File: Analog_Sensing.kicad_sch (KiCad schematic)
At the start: 3 parts, among them U12 TMP1075NDRLR

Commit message: Layout draft complete
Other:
- note removed: "Analog Inputs - NOT NEEDED"
- title: (none) -> Jakka1
- moved on the sheet: C60, R48, U12

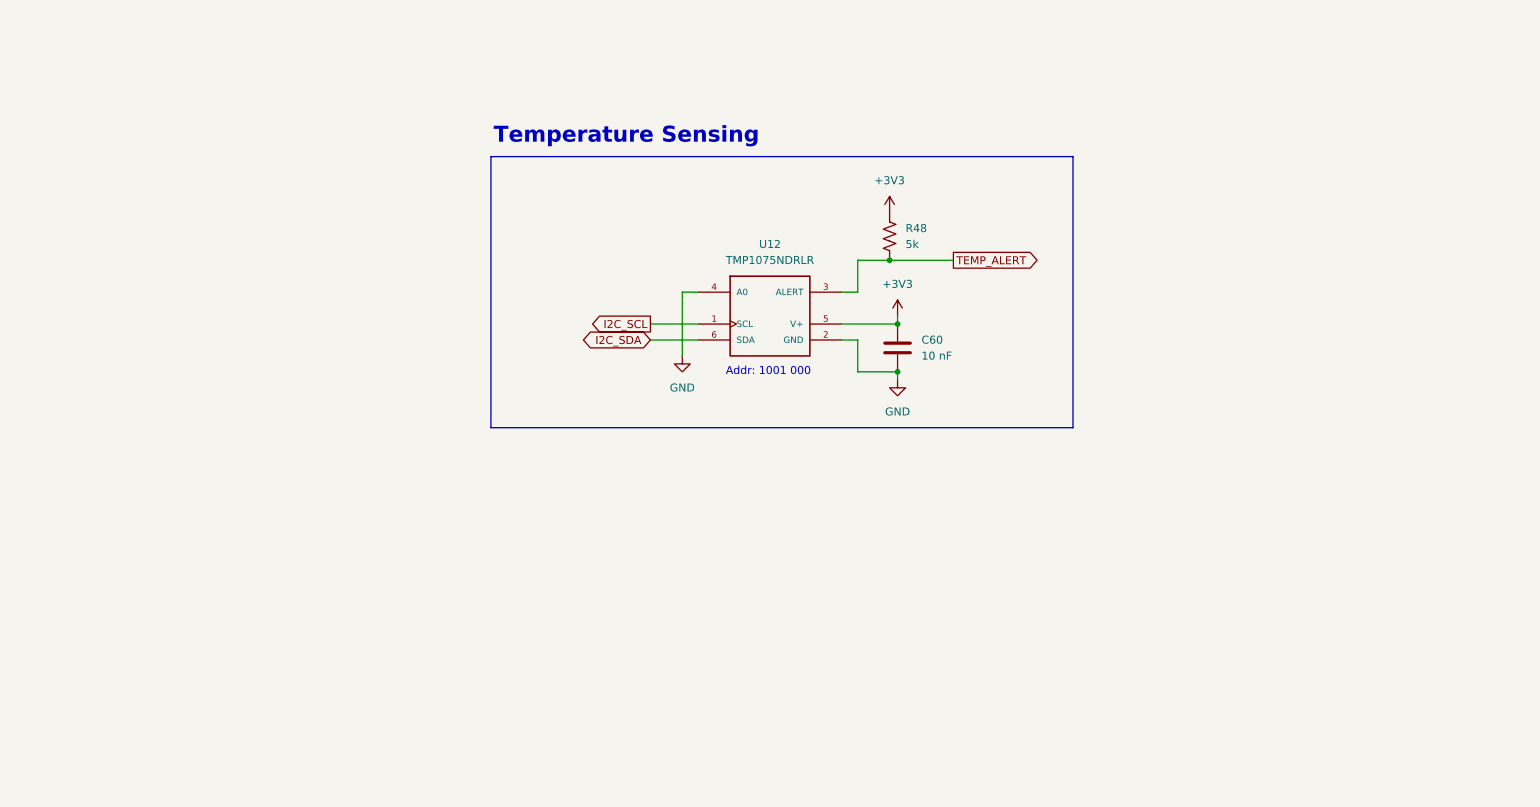
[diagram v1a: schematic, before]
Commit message: First draft of design output, schematic, and layout complete
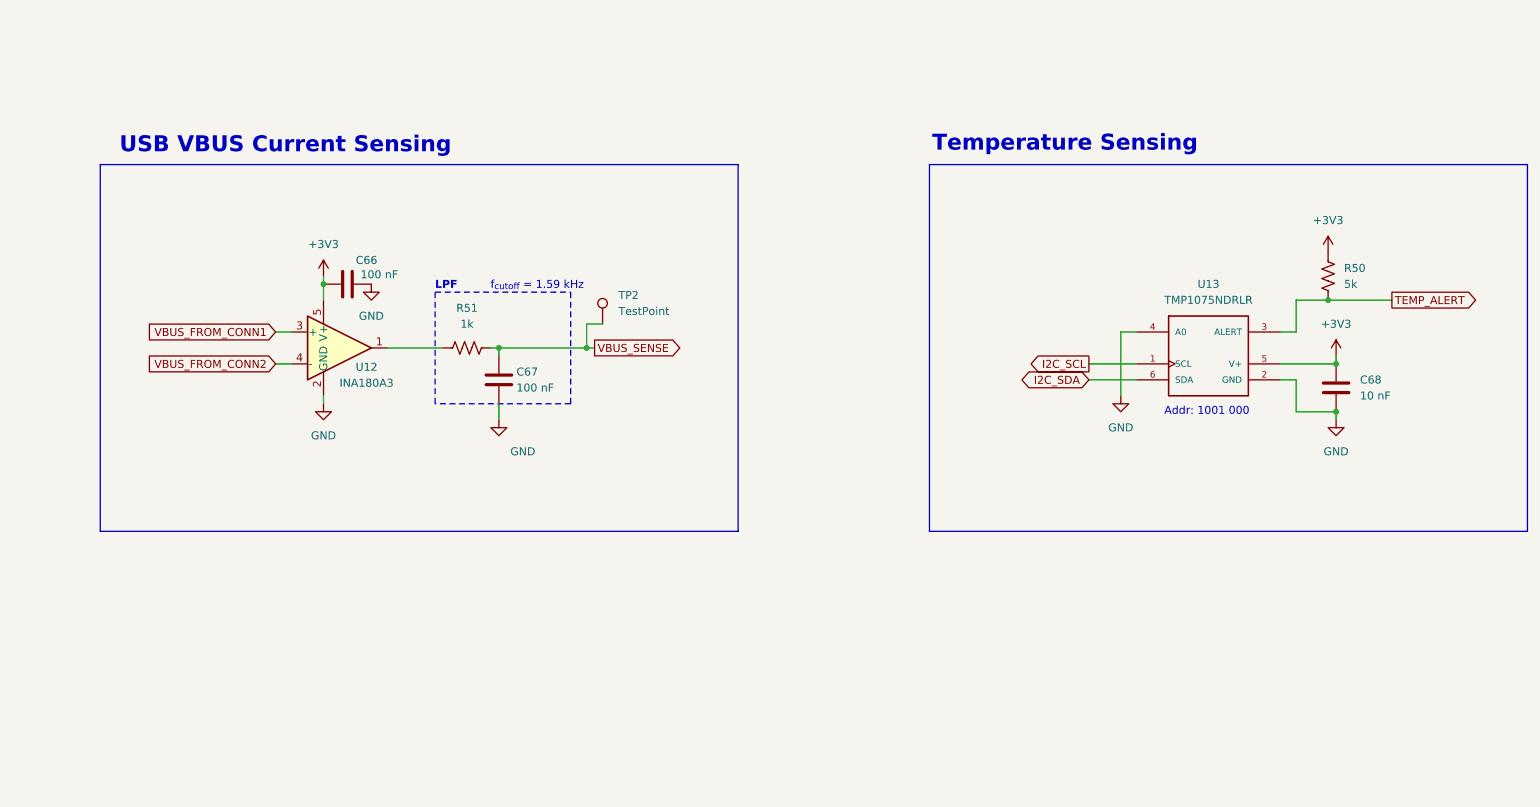
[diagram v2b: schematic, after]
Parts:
- added C66, C67: 100 nF, Capacitor_SMD:C_0603_1608Metric, symbol Device:C
- added R51: 1k, Resistor_SMD:R_0603_1608Metric, symbol Device:R_US
- added TP2: TestPoint, TestPoint:TestPoint_Pad_D1.0mm, symbol Connector:TestPoint
- added U12: INA180A3, Package_TO_SOT_SMD:SOT-23-5, symbol Amplifier_Current:INA180A1
- renumbered C60 to C68, R48 to R50, U12 to U13
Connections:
- net +3V3: now also C66.1, U12.5 (V+)
- net GND: now also C66.2, C67.1, U12.2 (GND)
- new net: R51.1, U12.1
- new net VBUS_FROM_CONN1: U12.3 (+)
- new net VBUS_FROM_CONN2: U12.4 (-)
- new net VBUS_SENSE: C67.2, R51.2, TP2.1
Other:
- note added: "LPF"
- note added: "USB VBUS Current Sensing"
- note added: "f_{cutoff} = 1.59 kHz"
- company: (none) -> Jacob Kapala
- moved on the sheet: C68, R50, U13
